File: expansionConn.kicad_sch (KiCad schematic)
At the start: 0 parts

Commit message: Add layout for expansion connector and M.2 key M slot
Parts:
- added C1, C2, C3, C4, C5: C_1u_0402, antmicro-footprints:C_0402_1005Metric, symbol antmicroCapacitors0402:C_1u_0402
- added J1: ERM8-040-05.0-L-DV-K-TR, antmicro-footprints:ERM8-040-05.0_SAMTEC, symbol antmicroB2bConnectors:J_ERM8-040-XX.X-X-DV-XX_SAMTEC
- added R1, R2: R_0R_0603, antmicro-footprints:R_0603_1608Metric, symbol antmicroResistors0603:R_0R_0603
- added TP1, TP2, TP3: TP_1.5mm_SMD, antmicro-footprints:TP_SMD_1.5mm, symbol antmicroTestPoints:TP_1.5mm_SMD
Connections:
- new net: C5.2, J1.74, R2.1
- new net +3V3: R1.1
- new net 12V_CONN: C4.2, J1.78, J1.80, TP3.1
- new net 1V8_CONN: C2.2, J1.73, TP1.1
- new net 3V3_CONN: C1.2, J1.67, J1.69, R1.2
- new net 3V3_STDB: R2.2
- new net 5V_CONN: C3.2, J1.77, J1.79, TP2.1
- new net CAN_RX: J1.68
- new net CAN_TX: J1.70
- new net GND: C1.1, C2.1, C3.1, C4.1, C5.1, J1.01, J1.02, J1.04, J1.07, J1.10, J1.13, J1.16, J1.19, J1.22, J1.25, J1.28, J1.37, J1.38, J1.49, J1.50, J1.61, J1.62, J1.71, J1.72, J1.75, J1.76
- new net GPIO01: J1.31
- new net GPIO07: J1.33
- new net GPIO09: J1.35
- new net GPIO11: J1.42
- new net GPIO12: J1.40
- new net GPIO13: J1.36
- new net I2C2_SCL: J1.66
- new net I2C2_SDA: J1.64
- new net I2S0_LRCK: J1.47
- new net I2S0_SCLK: J1.46
- new net I2S0_SDIN: J1.45
- new net I2S0_SDOUT: J1.48
- new net PCIE2_CLKREQ: J1.29
- new net PCIE2_CLK_N: J1.15
- new net PCIE2_CLK_P: J1.17
- new net PCIE2_RST: J1.27
- new net PCIE2_RX0_N: J1.12
- new net PCIE2_RX0_P: J1.14
- new net PCIE2_RX1_N: J1.06
- new net PCIE2_RX1_P: J1.08
- new net PCIE2_TX0_N: J1.09
- new net PCIE2_TX0_P: J1.11
- new net PCIE2_TX1_N: J1.03
- new net PCIE2_TX1_P: J1.05
- new net PCIE3_CLKREQ*: J1.32
- new net PCIE3_CLK_N: J1.18
- new net PCIE3_CLK_P: J1.20
- new net PCIE3_RST*: J1.30
- new net PCIE_WAKE_SEL_EXT_CONN: J1.34
- new net SPI0_MISO: J1.55
- new net SPI0_MOSI: J1.53
- new net SPI0_SCK: J1.51
- new net SPI1_MISO: J1.56
- new net SPI1_MOSI: J1.54
- new net SPI1_SCK: J1.52
- new net SYS_SCL: J1.65
- new net SYS_SDA: J1.63
- new net UART1_RXD: J1.39
- new net UART1_TXD: J1.44
- new net USB1_D_N: J1.41
- new net USB1_D_P: J1.43
- new net USBSS1_RX_N: J1.24
- new net USBSS1_RX_P: J1.26
- new net USBSS1_TX_N: J1.21
- new net USBSS1_TX_P: J1.23
- new net ~{SPI0_CS0}: J1.57
- new net ~{SPI0_CS1}: J1.59
- new net ~{SPI1_CS0}: J1.58
- new net ~{SPI1_CS1}: J1.60
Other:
- note added: "Expansion connector"
- note added: "LOW POWER ONLY FOR LEVEL SHIFTERS"

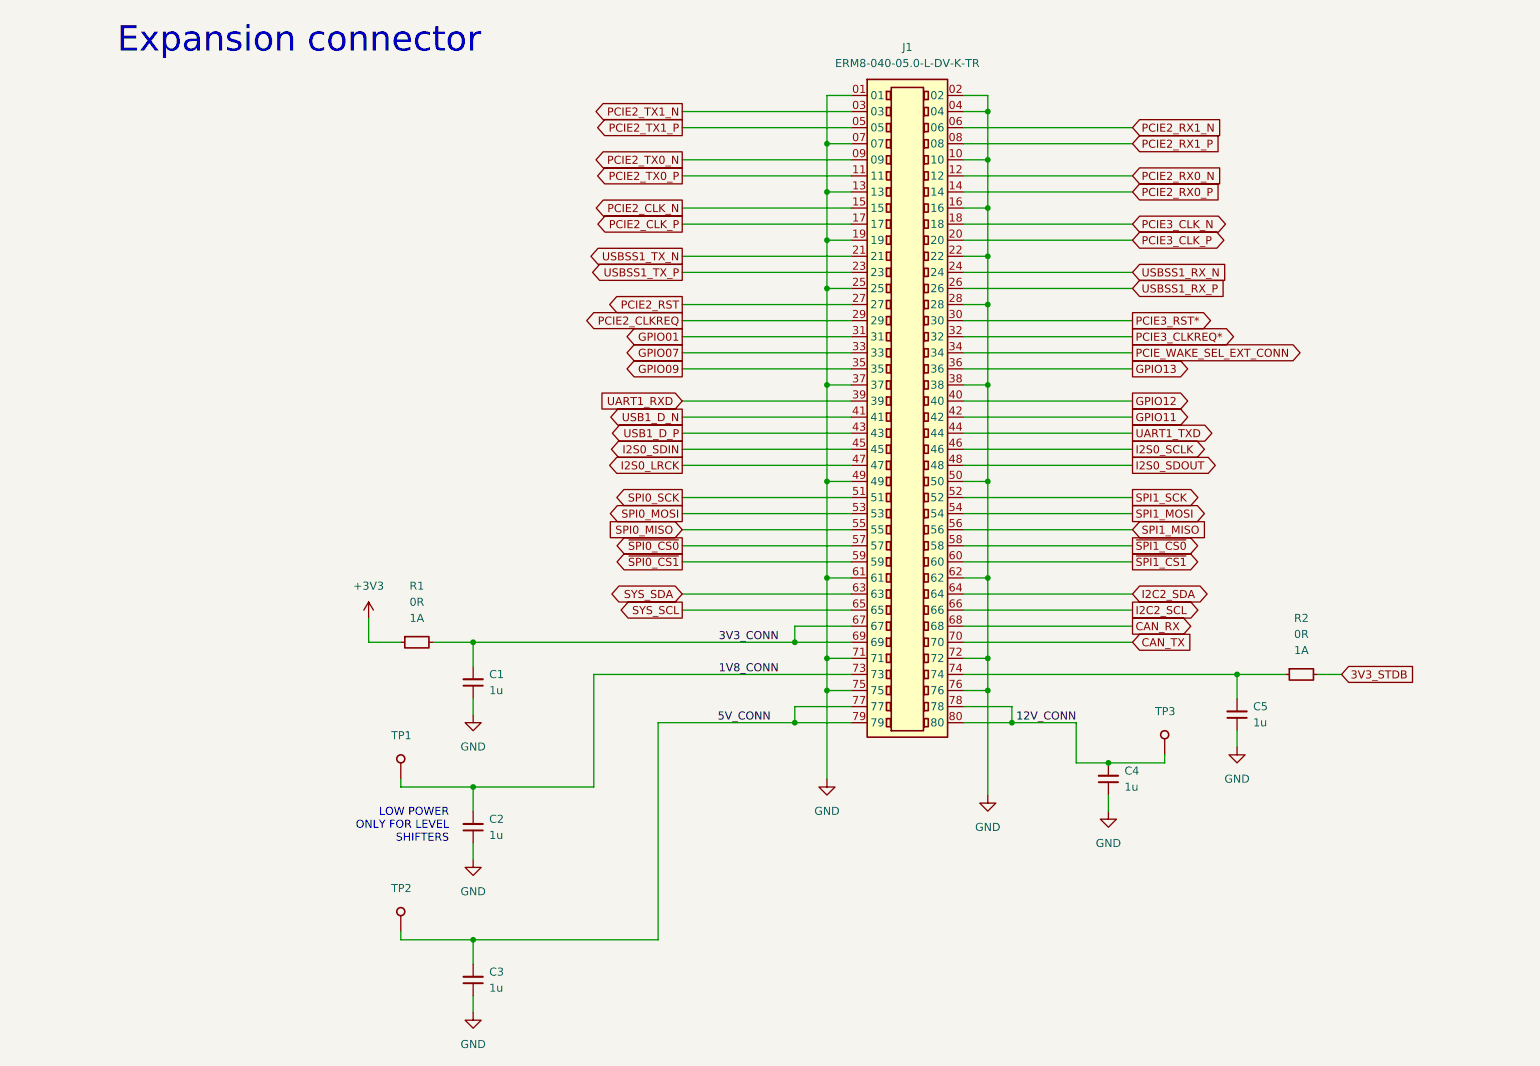
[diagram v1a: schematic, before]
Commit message: [#45539] Finish schematic + draw dif pairs and other signals
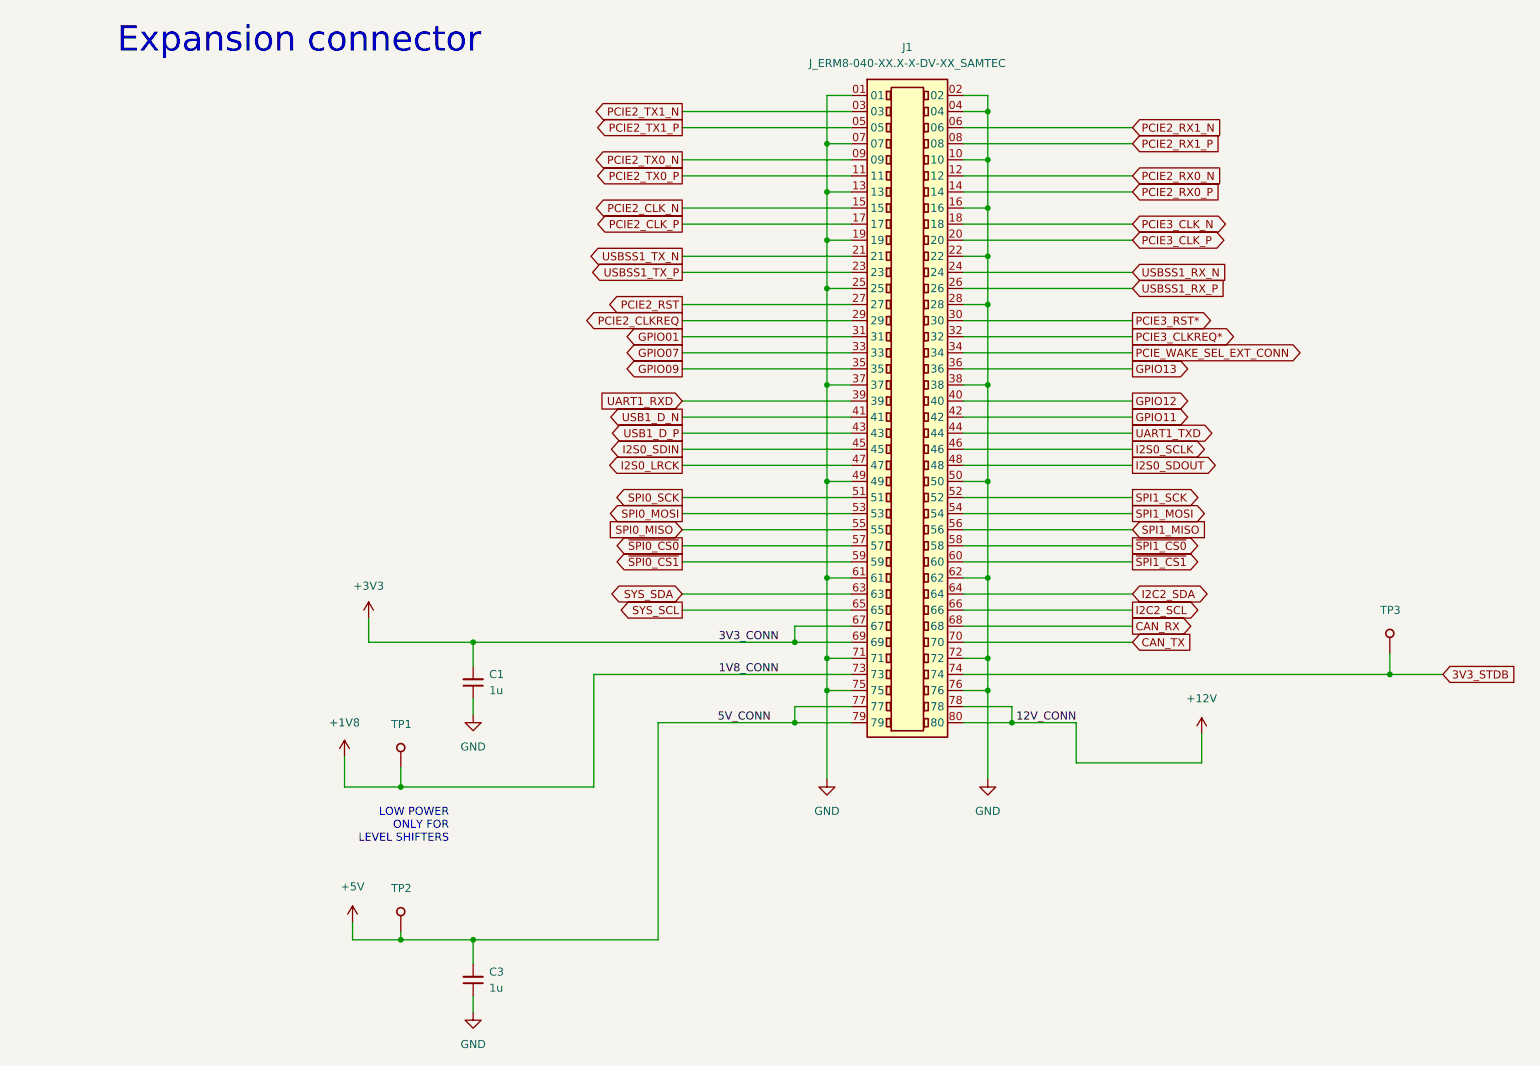
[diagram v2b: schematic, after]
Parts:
- removed C2, C4, C5: C_1u_0402, antmicro-footprints:C_0402_1005Metric, symbol antmicroCapacitors0402:C_1u_0402
- removed R1, R2: R_0R_0603, antmicro-footprints:R_0603_1608Metric, symbol antmicroResistors0603:R_0R_0603
- J1: value ERM8-040-05.0-L-DV-K-TR -> J_ERM8-040-XX.X-X-DV-XX_SAMTEC
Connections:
- net 3V3_CONN is gone; now on net +3V3: C1.2, J1.67, J1.69
- net 3V3_STDB: now also J1.74, TP3.1
- net 12V_CONN renamed +12V
- net +12V: no longer TP3.1
- net 1V8_CONN renamed +1V8
- net 5V_CONN renamed +5V

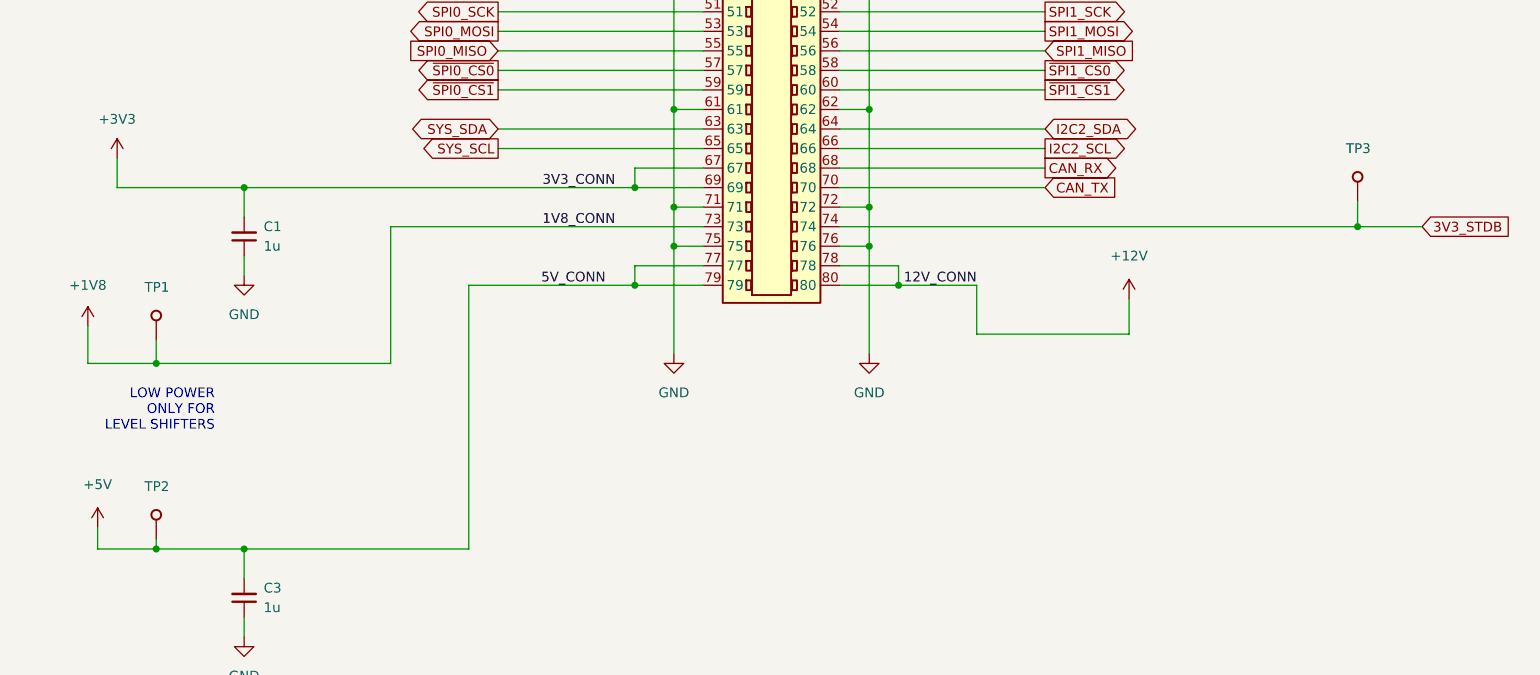
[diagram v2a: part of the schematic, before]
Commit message: [#45539] Change spacing of the m2 spacers, fix DRC, prepare labels for sd card reader
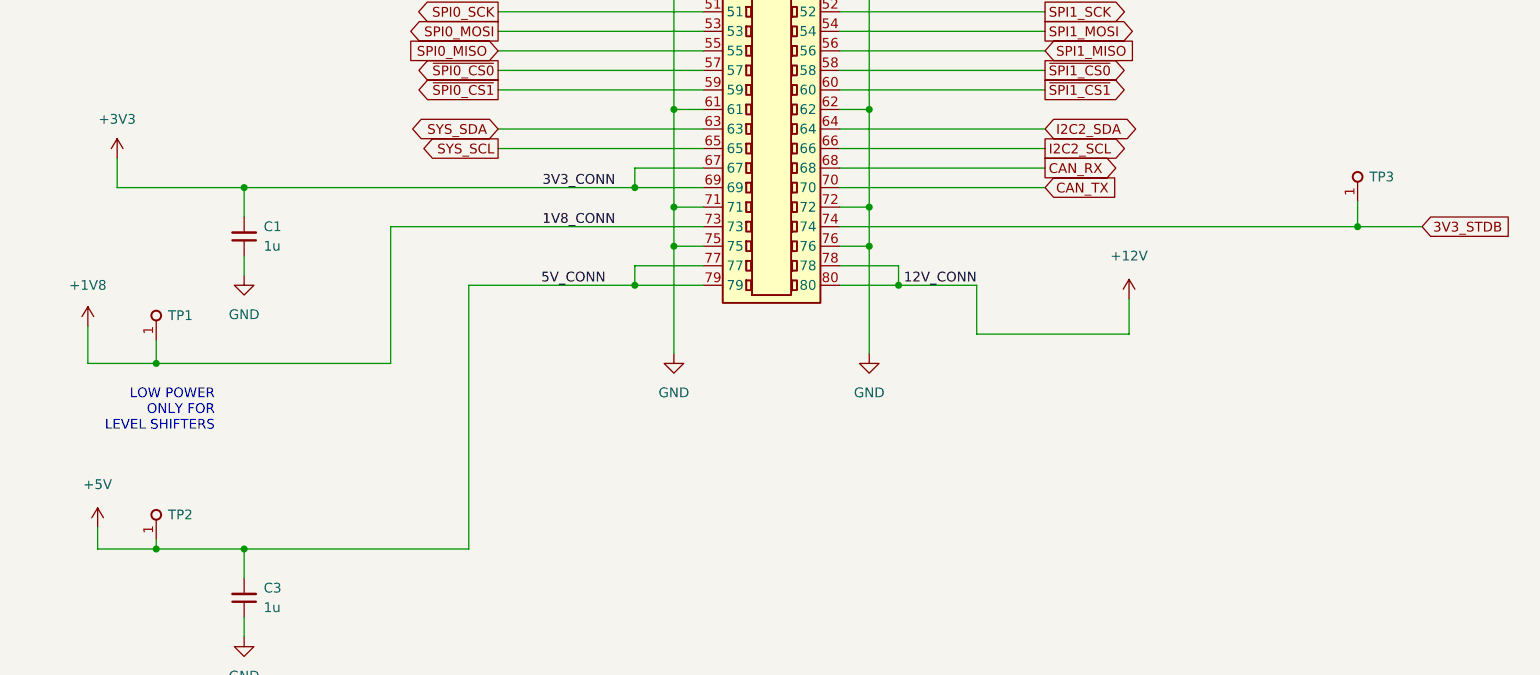
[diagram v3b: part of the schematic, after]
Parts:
- removed TP1, TP2, TP3: TP_1.5mm_SMD, antmicro-footprints:TP_SMD_1.5mm, symbol antmicroTestPoints:TP_1.5mm_SMD
- added TP1, TP2, TP3: TP_0.75mm_SMD, antmicro-footprints:TP_SMD_0.75mm, symbol antmicroTestPoints:TP_0.75mm_SMD
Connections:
- net +1V8: now also TP1.1
- net +5V: now also TP2.1
- net 3V3_STDB: now also TP3.1
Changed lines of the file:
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@@
-    (pin "1")
-  )
-  (symbol (lib_id "antmicroTestPoints:TP_1.5mm_SMD") (at 63.5 132.842 90) (unit 1)
-    (in_bom yes) (on_board yes)
-    (property "Reference" "TP1" (id 0) (at 61.976 125.984 90)
-      (effects (font (size 1.27 1.27) (thickness 0.15)) (justify right))
-    )
-    (property "Value" "TP_1.5mm_SMD" (id 1) (at 56.134 127.762 90)
-      (effects (font (size 1.27 1.27) (thickness 0.15)) (justify right) hide)
-    )
-    (property "Footprint" "antmicro-footprints:TP_SMD_1.5mm" (id 2) (at 73.66 117.602 0)
-      (effects (font (size 1.27 1.27) (thickness 0.15)) (justify left bottom) hide)
-    )
-    (property "Datasheet" "" (id 3) (at 76.2 117.602 0)
-      (effects (font (size 1.27 1.27) (thickness 0.15)) (justify left bottom) hide)
-    )
-    (property "MPN" "" (id 4) (at 63.5 132.842 0)
-      (effects (font (size 1.27 1.27)) hide)
-    )
-    (property "Manufacturer" "" (id 5) (at 63.5 132.842 0)
-      (effects (font (size 1.27 1.27)) hide)
-    )
-    (property "Author" "Antmicro" (id 6) (at 78.74 117.602 0)
-      (effects (font (size 1.27 1.27) (thickness 0.15)) (justify left bottom) hide)
-    )
-    (property "License" "Apache-2.0" (id 7) (at 81.28 117.602 0)
-      (effects (font (size 1.27 1.27) (thickness 0.15)) (justify left bottom) hide)
-    )
     (pin "1")
   )
@@
     (pin "1")
   )
-  (symbol (lib_id "antmicroTestPoints:TP_1.5mm_SMD") (at 219.71 114.808 90) (unit 1)
-    (in_bom yes) (on_board yes)
-    (property "Reference" "TP3" (id 0) (at 218.186 107.95 90)
-      (effects (font (size 1.27 1.27) (thickness 0.15)) (justify right))
-    )
-    (property "Value" "TP_1.5mm_SMD" (id 1) (at 212.344 109.728 90)
-      (effects (font (size 1.27 1.27) (thickness 0.15)) (justify right) hide)
-    )
-    (property "Footprint" "antmicro-footprints:TP_SMD_1.5mm" (id 2) (at 229.87 99.568 0)
-      (effects (font (size 1.27 1.27) (thickness 0.15)) (justify left bottom) hide)
-    )
-    (property "Datasheet" "" (id 3) (at 232.41 99.568 0)
-      (effects (font (size 1.27 1.27) (thickness 0.15)) (justify left bottom) hide)
-    )
-    (property "MPN" "" (id 4) (at 219.71 114.808 0)
-      (effects (font (size 1.27 1.27)) hide)
-    )
-    (property "Manufacturer" "" (id 5) (at 219.71 114.808 0)
-      (effects (font (size 1.27 1.27)) hide)
-    )
-    (property "Author" "Antmicro" (id 6) (at 234.95 99.568 0)
-      (effects (font (size 1.27 1.27) (thickness 0.15)) (justify left bottom) hide)
-    )
-    (property "License" "Apache-2.0" (id 7) (at 237.49 99.568 0)
-      (effects (font (size 1.27 1.27) (thickness 0.15)) (justify left bottom) hide)
-    )
-    (pin "1")
-  )
-  (symbol (lib_id "antmicroTestPoints:TP_1.5mm_SMD") (at 63.5 158.75 90) (unit 1)
-    (in_bom yes) (on_board yes)
-    (property "Reference" "TP2" (id 0) (at 61.976 151.892 90)
-      (effects (font (size 1.27 1.27) (thickness 0.15)) (justify right))
-    )
-    (property "Value" "TP_1.5mm_SMD" (id 1) (at 56.134 153.67 90)
-      (effects (font (size 1.27 1.27) (thickness 0.15)) (justify right) hide)
-    )
-    (property "Footprint" "antmicro-footprints:TP_SMD_1.5mm" (id 2) (at 73.66 143.51 0)
-      (effects (font (size 1.27 1.27) (thickness 0.15)) (justify left bottom) hide)
-    )
-    (property "Datasheet" "" (id 3) (at 76.2 143.51 0)
-      (effects (font (size 1.27 1.27) (thickness 0.15)) (justify left bottom) hide)
-    )
-    (property "MPN" "" (id 4) (at 63.5 158.75 0)
-      (effects (font (size 1.27 1.27)) hide)
-    )
-    (property "Manufacturer" "" (id 5) (at 63.5 158.75 0)
-      (effects (font (size 1.27 1.27)) hide)
-    )
-    (property "Author" "Antmicro" (id 6) (at 78.74 143.51 0)
-      (effects (font (size 1.27 1.27) (thickness 0.15)) (justify left bottom) hide)
-    )
-    (property "License" "Apache-2.0" (id 7) (at 81.28 143.51 0)
+  (symbol (lib_id "antmicroTestPoints:TP_0.75mm_SMD") (at 63.5 132.842 90) (unit 1)
+    (in_bom yes) (on_board yes) (fields_autoplaced)
+    (property "Reference" "TP1" (id 0) (at 65.024 129.6669 90)
+      (effects (font (size 1.27 1.27) (thickness 0.15)) (justify right))
+    )
+    (property "Value" "TP_0.75mm_SMD" (id 1) (at 71.12 117.602 0)
+      (effects (font (size 1.27 1.27) (thickness 0.15)) (justify left bottom) hide)
+    )
+    (property "Footprint" "antmicro-footprints:TP_SMD_0.75mm" (id 2) (at 73.66 117.602 0)
+      (effects (font (size 1.27 1.27) (thickness 0.15)) (justify left bottom) hide)
+    )
+    (property "Datasheet" "" (id 3) (at 76.2 117.602 0)
+      (effects (font (size 1.27 1.27) (thickness 0.15)) (justify left bottom) hide)
+    )
+    (property "MPN" "" (id 4) (at 63.5 132.842 0)
+      (effects (font (size 1.27 1.27)) hide)
+    )
+    (property "Manufacturer" "" (id 5) (at 63.5 132.842 0)
+      (effects (font (size 1.27 1.27)) hide)
+    )
+    (property "Author" "Antmicro" (id 6) (at 78.74 117.602 0)
+      (effects (font (size 1.27 1.27) (thickness 0.15)) (justify left bottom) hide)
+    )
+    (property "License" "Apache-2.0" (id 7) (at 81.28 117.602 0)
       (effects (font (size 1.27 1.27) (thickness 0.15)) (justify left bottom) hide)
     )
@@
     )
     (pin "1")
+  )
+  (symbol (lib_id "antmicroTestPoints:TP_0.75mm_SMD") (at 219.71 114.808 90) (unit 1)
+    (in_bom yes) (on_board yes) (fields_autoplaced)
+    (property "Reference" "TP3" (id 0) (at 221.234 111.6329 90)
+      (effects (font (size 1.27 1.27) (thickness 0.15)) (justify right))
+    )
+    (property "Value" "TP_0.75mm_SMD" (id 1) (at 227.33 99.568 0)
+      (effects (font (size 1.27 1.27) (thickness 0.15)) (justify left bottom) hide)
+    )
+    (property "Footprint" "antmicro-footprints:TP_SMD_0.75mm" (id 2) (at 229.87 99.568 0)
+      (effects (font (size 1.27 1.27) (thickness 0.15)) (justify left bottom) hide)
+    )
+    (property "Datasheet" "" (id 3) (at 232.41 99.568 0)
+      (effects (font (size 1.27 1.27) (thickness 0.15)) (justify left bottom) hide)
+    )
+    (property "MPN" "" (id 4) (at 219.71 114.808 0)
+      (effects (font (size 1.27 1.27)) hide)
+    )
+    (property "Manufacturer" "" (id 5) (at 219.71 114.808 0)
+      (effects (font (size 1.27 1.27)) hide)
+    )
+    (property "Author" "Antmicro" (id 6) (at 234.95 99.568 0)
+      (effects (font (size 1.27 1.27) (thickness 0.15)) (justify left bottom) hide)
+    )
+    (property "License" "Apache-2.0" (id 7) (at 237.49 99.568 0)
+      (effects (font (size 1.27 1.27) (thickness 0.15)) (justify left bottom) hide)
+    )
+    (pin "1")
+  )
+  (symbol (lib_id "antmicroTestPoints:TP_0.75mm_SMD") (at 63.5 158.75 90) (unit 1)
+    (in_bom yes) (on_board yes) (fields_autoplaced)
+    (property "Reference" "TP2" (id 0) (at 65.024 155.5749 90)
+      (effects (font (size 1.27 1.27) (thickness 0.15)) (justify right))
+    )
+    (property "Value" "TP_0.75mm_SMD" (id 1) (at 71.12 143.51 0)
+      (effects (font (size 1.27 1.27) (thickness 0.15)) (justify left bottom) hide)
+    )
+    (property "Footprint" "antmicro-footprints:TP_SMD_0.75mm" (id 2) (at 73.66 143.51 0)
+      (effects (font (size 1.27 1.27) (thickness 0.15)) (justify left bottom) hide)
+    )
+    (property "Datasheet" "" (id 3) (at 76.2 143.51 0)
+      (effects (font (size 1.27 1.27) (thickness 0.15)) (justify left bottom) hide)
+    )
+    (property "MPN" "" (id 4) (at 63.5 158.75 0)
+      (effects (font (size 1.27 1.27)) hide)
+    )
+    (property "Manufacturer" "" (id 5) (at 63.5 158.75 0)
+      (effects (font (size 1.27 1.27)) hide)
+    )
+    (property "Author" "Antmicro" (id 6) (at 78.74 143.51 0)
+      (effects (font (size 1.27 1.27) (thickness 0.15)) (justify left bottom) hide)
+    )
+    (property "License" "Apache-2.0" (id 7) (at 81.28 143.51 0)
+      (effects (font (size 1.27 1.27) (thickness 0.15)) (justify left bottom) hide)
+    )
+    (pin "1")
